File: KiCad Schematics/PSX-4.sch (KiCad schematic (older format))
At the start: 25 parts

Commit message: Updated schematic
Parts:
- added APP?: Gray, symbol CONN-1
- APP?: value Green -> Red
- APP?: value Red -> Green
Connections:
- net at PSX?.J1-3 (DCC2): no longer TB?.1 (P1)
- net at PSX?.J1-4 (DCC1): no longer TB?.1 (P1)
- net Green: now reaches PSX?.J2-1 (DCC2), TB8.2 (P2)
- net Green: now also APP?.1 (P1), PSX?.J1-2 (Daisy2), TB?.1 (P1)
- net Red: now reaches PSX?.J2-2 (DCC1), TB8.1 (P1)
- net Red: now also APP?.1 (P1), PSX?.J1-1 (Daisy1), TB?.1 (P1)
- net Yellow: now reaches PSX?.J2-1 (DCC2), TB8.4 (P4)
- net Yellow: now also APP?.1 (P1)
- net Blue: now reaches PSX?.J2-2 (DCC1), TB8.3 (P3)
- net Blue: now also APP?.1 (P1)
- net Brown: now reaches PSX?.J2-1 (DCC2), TB8.6 (P6)
- net Brown: now also APP?.1 (P1), APP?.1 (P1), PSX?.J2-1 (DCC2), TB8.8 (P8)
- net Orange: now reaches PSX?.J2-2 (DCC1), TB8.5 (P5)
- net Orange: now also APP?.1 (P1), APP?.1 (P1), PSX?.J2-2 (DCC1), TB8.7 (P7)
- net at APP?.1 (P1): now also TB?.1 (P1); no longer TB?.1 (P1) (x4)
- no-connect marks 2 -> 3
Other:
- note added: "Anderson PP block\nto yard sub-district 4\nand local AC accessory"
- note added: "Anderson PP block\nto yard sub-districts 1-3\nand local AC accessory"
- note removed: "Anderson PP block\nto sub-district 4\nand AC accessory"
- note removed: "Anderson PP block\nto sub-districts 1-3\nand yard AC accessory"

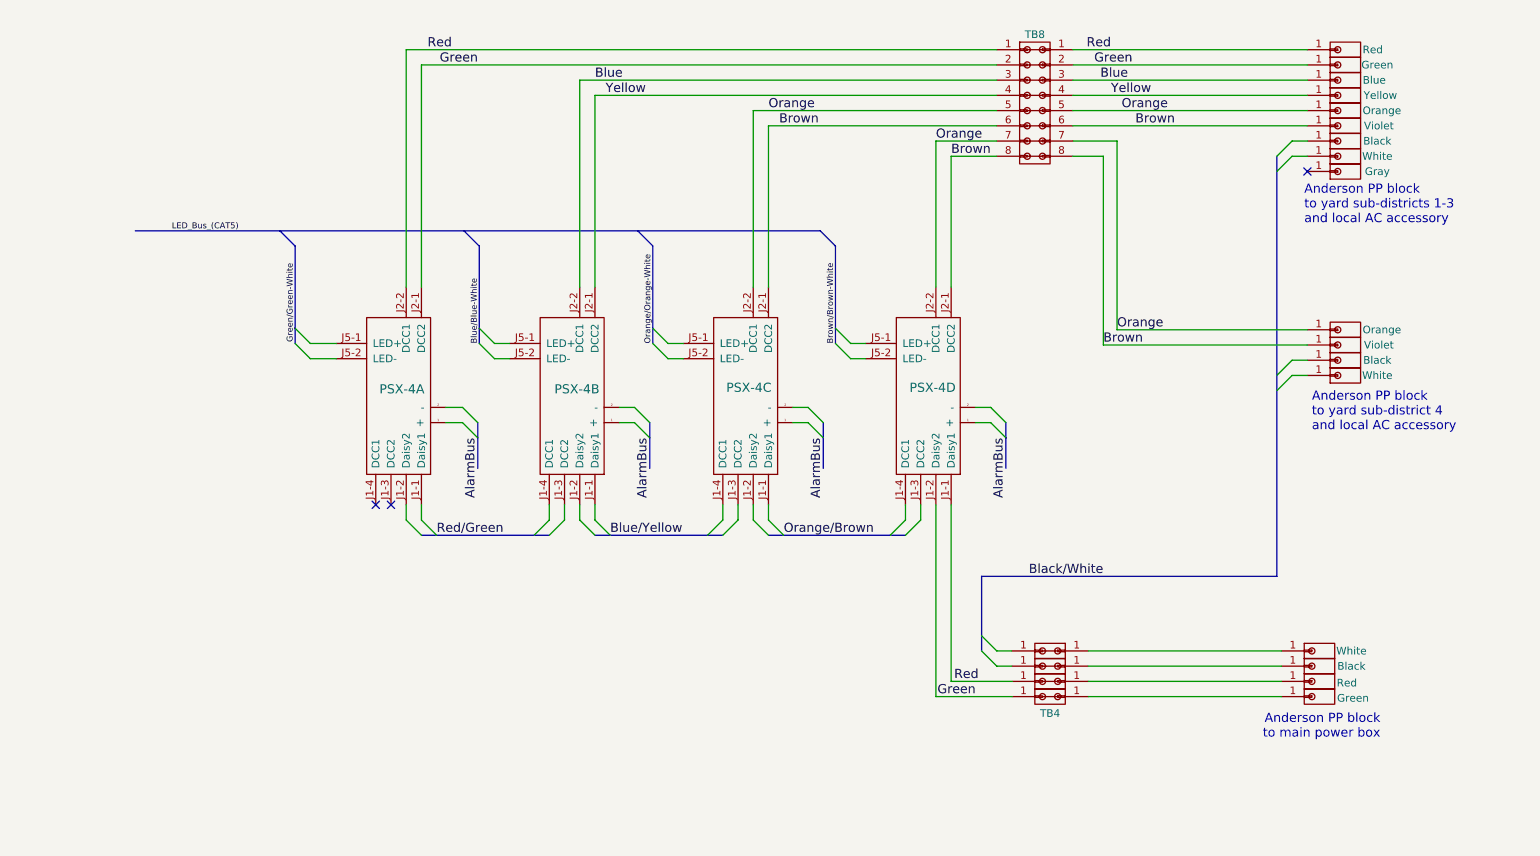
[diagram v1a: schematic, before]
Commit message: Simplified schematic
Added heirarchy sheets to simplify the schematic.
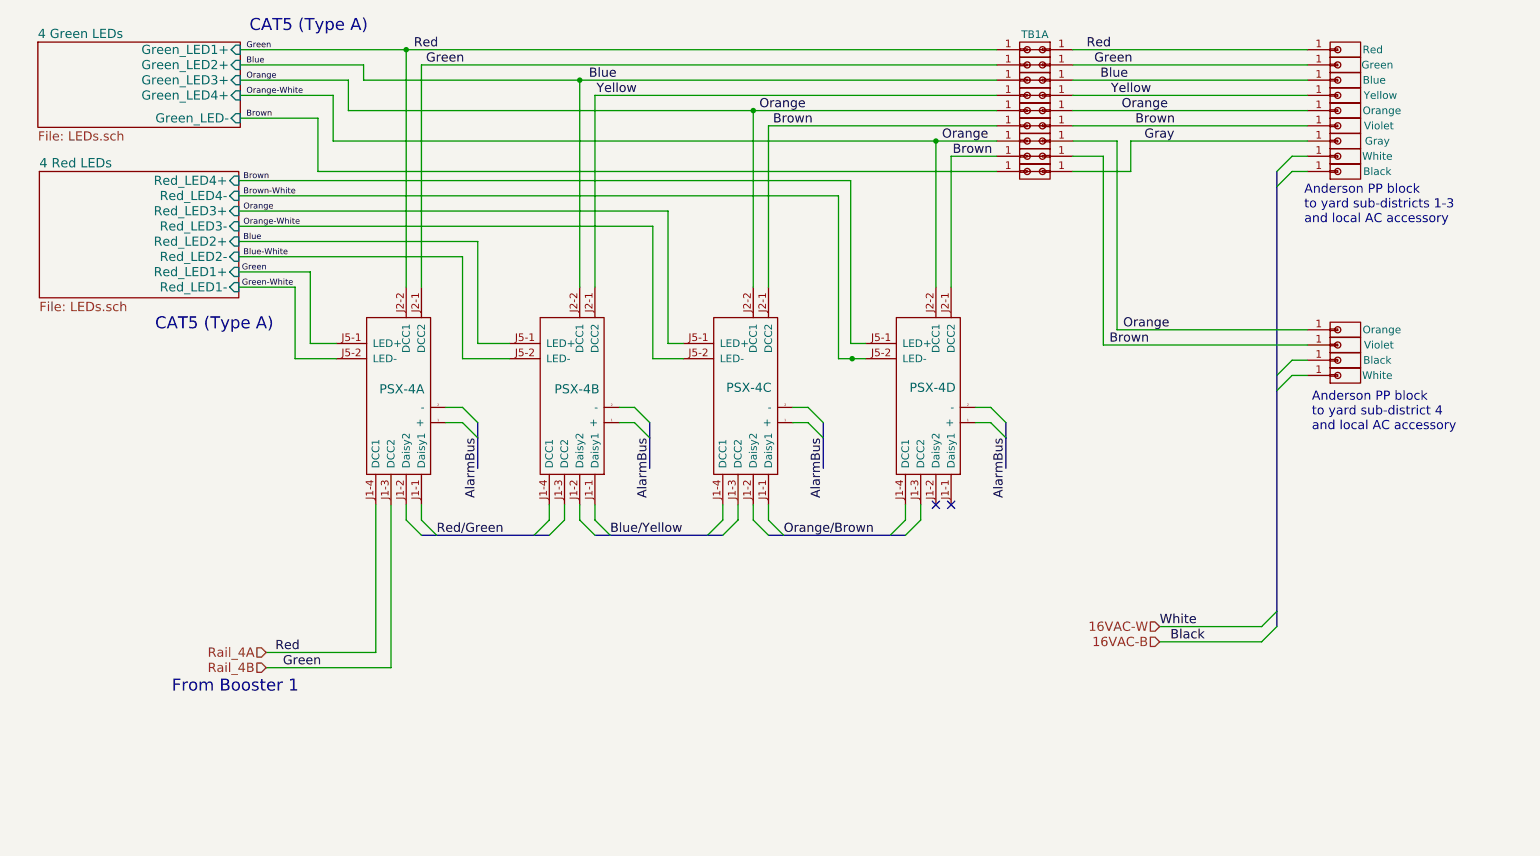
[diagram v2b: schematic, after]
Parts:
- removed APP?: Red, symbol CONN-1
- removed APP?: Green, symbol CONN-1
- removed APP?: Black, symbol CONN-1
- removed APP?: White, symbol CONN-1
- removed TB8: TERM_08, symbol TERM_08
- removed TB?: TB4, symbol TBLOCK
- removed TB? (x3): TBLOCK, symbol TBLOCK
- added TB1, TB? (x8): TBLOCK, symbol TBLOCK
- APP?: value Black -> Gray
- APP?: value Gray -> Black
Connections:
- net Blue: now also PSX?.J5-1 (LED+), TB?.1 (P1)
- net Brown: now also PSX?.J5-1 (LED+), TB?.1 (P1), TB?.1 (P1), TB?.1 (P1)
- net Orange: now also PSX?.J5-1 (LED+), PSX?.J5-2 (LED-), TB?.1 (P1), TB?.1 (P1)
- net Yellow: now also TB?.1 (P1)
- net Rail_4A: now reaches PSX?.J1-3 (DCC2)
- net Rail_4A: now also APP?.1 (P1), APP?.1 (P1), PSX?.J1-4 (DCC1), PSX?.J2-1 (DCC2), PSX?.J2-2 (DCC1), PSX?.J5-1 (LED+), TB1.1 (P1), TB?.1 (P1)
- net Green-White: now reaches PSX?.J5-2 (LED-)
- net Blue-White: now reaches PSX?.J5-2 (LED-)
- net Brown-White: now reaches PSX?.J5-2 (LED-)
- net Gray: now reaches APP?.1 (P1)
- net Gray: now also TB?.1 (P1)
- removed net Green: APP?.1 (P1), PSX?.J1-2 (Daisy2), PSX?.J2-1 (DCC2)
- removed net Red: APP?.1 (P1), PSX?.J1-1 (Daisy1), PSX?.J2-2 (DCC1)
- no-connect marks 3 -> 2
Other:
- note added: "CAT5 (Type A)"
- note added: "From Booster 1"
- note removed: "Anderson PP block\nto main power box"
